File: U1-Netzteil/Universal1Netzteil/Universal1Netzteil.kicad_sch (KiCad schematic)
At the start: 13 parts, among them J1 Screw_Terminal_01x08, P1 Conn_Plug_2P

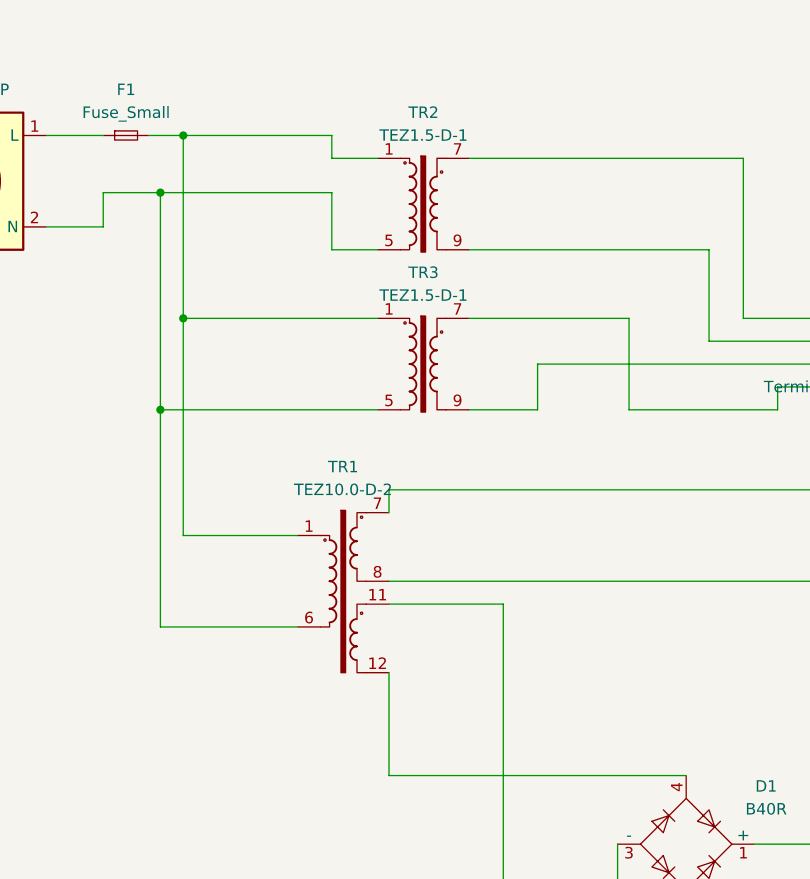
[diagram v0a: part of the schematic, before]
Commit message: Verschiedene Anpassungen in 2 Projekten. Netzteil Aufgebaut und OK. D-Amp funktioniert aber totes Ende im Projekt erreicht.
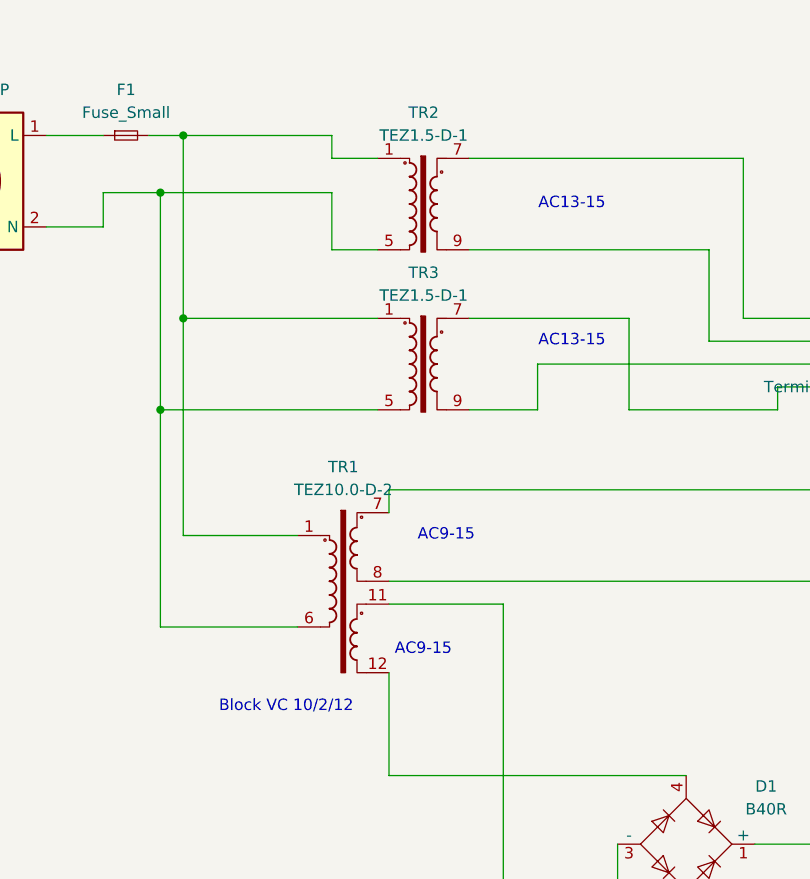
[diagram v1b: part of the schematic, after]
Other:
- note added: "AC13-15"
- note added: "AC9-15"
- note added: "Block VC 10/2/12"
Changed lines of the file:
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@@
 (kicad_sch
-	(version 20231120)
+	(version 20250114)
 	(generator "eeschema")
-	(generator_version "8.0")
+	(generator_version "9.0")
 	(paper "A4")
+	(text "AC13-15"
+		(exclude_from_sim no)
+		(at 105.41 63.5 0)
+		(effects
+			(font
+				(size 1.27 1.27)
+			)
+		)
+	)
+	(text "AC9-15"
+		(exclude_from_sim no)
+		(at 91.44 100.33 0)
+		(effects
+			(font
+				(size 1.27 1.27)
+			)
+		)
+	)
+	(text "Block VC 10/2/12 "
+		(exclude_from_sim no)
+		(at 73.66 119.38 0)
+		(effects
+			(font
+				(size 1.27 1.27)
+			)
+		)
+	)
+	(text "AC13-15"
+		(exclude_from_sim no)
+		(at 105.41 78.74 0)
+		(effects
+			(font
+				(size 1.27 1.27)
+			)
+		)
+	)
+	(text "AC9-15"
+		(exclude_from_sim no)
+		(at 88.9 113.03 0)
+		(effects
+			(font
+				(size 1.27 1.27)
+			)
+		)
+	)
 	(junction
 		(at 62.23 76.2)
@@
 		)
 	)
+	(embedded_fonts no)
 )
